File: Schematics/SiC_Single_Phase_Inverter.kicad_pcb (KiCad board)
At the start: 2 copper layers, 200 x 84 mm, 51 parts, among them J1 23AH8785-Black, J2 23AH8786-Red, Q1 STB10NK60ZT4, Q2 STB10NK60ZT4, Q3 C3M0025065K, Q4 C3M0025065K, Q5 C3M0025065K, Q6 C3M0025065K, Q7 C3M0025065K, U1 UCC21710QDWRQ1, U2 UCC21710QDWRQ1, U3 UCC21710QDWRQ1, U4 UCC21710QDWRQ1

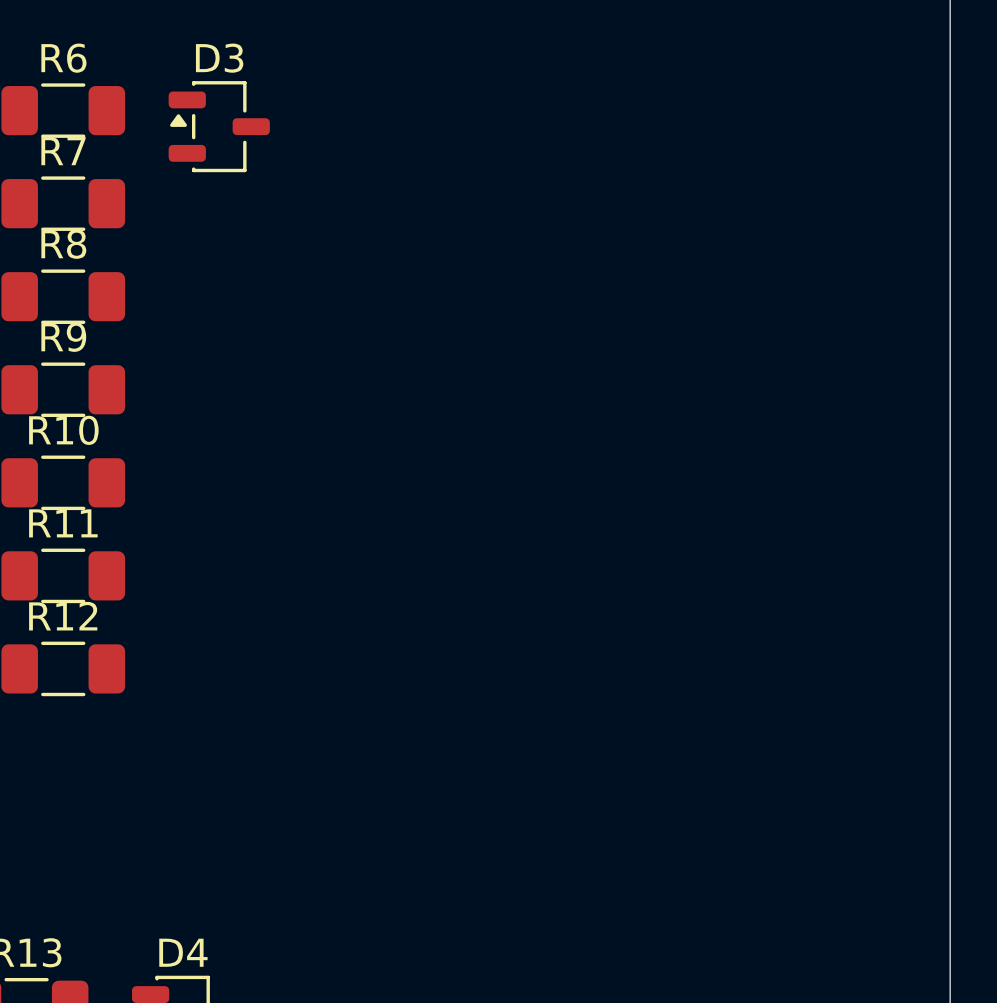
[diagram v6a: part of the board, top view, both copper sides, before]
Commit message: Copy past Leg A onto Leg B, Changed hames on both High/Low side to match Leg B
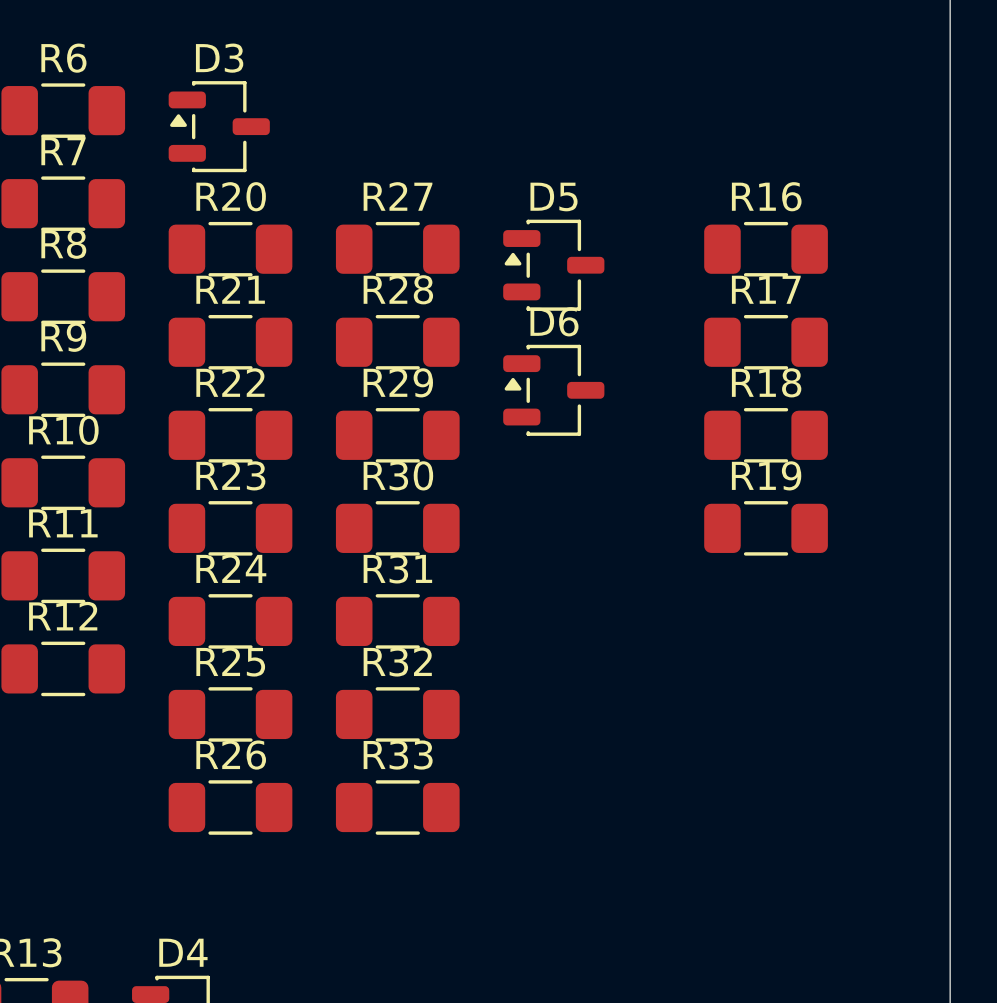
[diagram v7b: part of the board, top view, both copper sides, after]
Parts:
- added D5: BZX84C20-7-F, Package_TO_SOT_SMD:SOT-23-3, F.Cu at (255.9, 57.1)
- added D6: BZX84C20-7-F, Package_TO_SOT_SMD:SOT-23-3, F.Cu at (255.9, 61.6)
- added R16: 5K, Resistor_SMD:R_1206_3216Metric_Pad1.30x1.75mm_HandSolder, F.Cu at (263.4, 56.6)
- added R17: 5K, Resistor_SMD:R_1206_3216Metric_Pad1.30x1.75mm_HandSolder, F.Cu at (263.4, 59.9)
- added R18: 5K, Resistor_SMD:R_1206_3216Metric_Pad1.30x1.75mm_HandSolder, F.Cu at (263.4, 63.2)
- added R19: 5K, Resistor_SMD:R_1206_3216Metric_Pad1.30x1.75mm_HandSolder, F.Cu at (263.4, 66.5)
- added R20: 100K, Resistor_SMD:R_1206_3216Metric_Pad1.30x1.75mm_HandSolder, F.Cu at (244.4, 56.6)
- added R21: 100K, Resistor_SMD:R_1206_3216Metric_Pad1.30x1.75mm_HandSolder, F.Cu at (244.4, 59.9)
- added R22: 10, Resistor_SMD:R_1206_3216Metric_Pad1.30x1.75mm_HandSolder, F.Cu at (244.4, 63.2)
- added R23: 10, Resistor_SMD:R_1206_3216Metric_Pad1.30x1.75mm_HandSolder, F.Cu at (244.4, 66.5)
- added R24: 10, Resistor_SMD:R_1206_3216Metric_Pad1.30x1.75mm_HandSolder, F.Cu at (244.4, 69.8)
- added R25: 10, Resistor_SMD:R_1206_3216Metric_Pad1.30x1.75mm_HandSolder, F.Cu at (244.4, 73.1)
- added R26: 5K, Resistor_SMD:R_1206_3216Metric_Pad1.30x1.75mm_HandSolder, F.Cu at (244.4, 76.4)
- added R27: 100, Resistor_SMD:R_1206_3216Metric_Pad1.30x1.75mm_HandSolder, F.Cu at (250.3, 56.6)
- added R28: 5K, Resistor_SMD:R_1206_3216Metric_Pad1.30x1.75mm_HandSolder, F.Cu at (250.3, 59.9)
- added R29: 5K, Resistor_SMD:R_1206_3216Metric_Pad1.30x1.75mm_HandSolder, F.Cu at (250.3, 63.2)
- added R30: 100, Resistor_SMD:R_1206_3216Metric_Pad1.30x1.75mm_HandSolder, F.Cu at (250.3, 66.5)
- added R31: 5K, Resistor_SMD:R_1206_3216Metric_Pad1.30x1.75mm_HandSolder, F.Cu at (250.3, 69.8)
- added R32: 5K, Resistor_SMD:R_1206_3216Metric_Pad1.30x1.75mm_HandSolder, F.Cu at (250.3, 73.1)
- added R33: 5K, Resistor_SMD:R_1206_3216Metric_Pad1.30x1.75mm_HandSolder, F.Cu at (250.3, 76.4)
- R10, R12: value 10K -> 5K
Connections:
- D4 pad 2: GND -> GND_ISO_LALS
- Q4 pad 1: unconnected-(Q4-Pad1) -> /Full-Bridge/Leg_B_Power_Stage/BUS_DC+
- Q4 pad 2: unconnected-(Q4-Pad2) -> GND_ISO_LAHS
- Q4 pad 3: unconnected-(Q4-Pad3) -> GND_ISO_LAHS
- Q4 pad 4: Net-(Q4-Pad4) -> /Full-Bridge/Leg_B_Power_Stage/LegA_HS_Gate
- Q5 pad 1: unconnected-(Q5-Pad1) -> GND_ISO_LAHS
- Q5 pad 2: unconnected-(Q5-Pad2) -> GND_ISO_LALS
- Q5 pad 3: unconnected-(Q5-Pad3) -> GND_ISO_LALS
- Q5 pad 4: unconnected-(Q5-Pad4) -> /Full-Bridge/Leg_B_Power_Stage/LegA_LS_Gate
- Q7 pad 2: GND -> GND_ISO_LALS
- Q7 pad 3: GND -> GND_ISO_LALS
- R10 pad 1: /Full-Bridge/Leg_A_Power_Stage/LS_LegA_EN -> +3V3
- R10 pad 2: +3V3 -> /Full-Bridge/Leg_A_Power_Stage/LS_LegA_EN
- R12 pad 1: /Full-Bridge/Leg_A_Power_Stage/HS_LegA_EN -> +3V3
- R12 pad 2: +3V3 -> /Full-Bridge/Leg_A_Power_Stage/HS_LegA_EN
- R8 pad 2: GND -> GND_ISO_LALS
- U2 pad 1: GND -> GND_ISO_LALS
- U2 pad 2: GND -> GND_ISO_LALS
- U2 pad 3: GND -> GND_ISO_LALS
- U2 pad 5: +15V_LALS -> +15V_ISO_LALS
- U2 pad 8: /Full-Bridge/Leg_A_Power_Stage/GND_ISO_LALS -> GND_ISO_LALS
- U3 pad 1: unconnected-(U3-AIN-Pad1) -> GND_ISO_LALS
- U3 pad 10: unconnected-(U3-IN+-Pad10) -> Net-(U3-IN+)
- U3 pad 11: unconnected-(U3-IN--Pad11) -> LOGIC_GND
- U3 pad 12: unconnected-(U3-RDY-Pad12) -> /Full-Bridge/Leg_B_Power_Stage/LS_LegB_RDY
- U3 pad 13: unconnected-(U3-~{FLT}-Pad13) -> /Full-Bridge/Leg_B_Power_Stage/~{LS_LegB_FLT}
- U3 pad 14: unconnected-(U3-~{RST}/EN-Pad14) -> /Full-Bridge/Leg_B_Power_Stage/LS_LegB_EN
- U3 pad 15: unconnected-(U3-VCC-Pad15) -> +3V3
- U3 pad 2: unconnected-(U3-OC-Pad2) -> GND_ISO_LALS
- U3 pad 3: unconnected-(U3-COM-Pad3) -> GND_ISO_LALS
- U3 pad 4: unconnected-(U3-OUTH-Pad4) -> /Full-Bridge/Leg_B_Power_Stage/LegA_LS_OUTH
- U3 pad 5: unconnected-(U3-VDD-Pad5) -> +15V_ISO_LALS
- U3 pad 6: unconnected-(U3-OUTL-Pad6) -> /Full-Bridge/Leg_B_Power_Stage/LegA_LS_OUTL
- U3 pad 7: unconnected-(U3-CLMPI-Pad7) -> /Full-Bridge/Leg_B_Power_Stage/LegA_LS_Gate
- U3 pad 8: unconnected-(U3-VEE-Pad8) -> GND_ISO_LALS
- U3 pad 9: unconnected-(U3-GND-Pad9) -> LOGIC_GND
- U4 pad 1: unconnected-(U4-AIN-Pad1) -> GND_ISO_LAHS
- U4 pad 10: unconnected-(U4-IN+-Pad10) -> Net-(U4-IN+)
- U4 pad 11: unconnected-(U4-IN--Pad11) -> LOGIC_GND
- U4 pad 12: unconnected-(U4-RDY-Pad12) -> /Full-Bridge/Leg_B_Power_Stage/HS_LegB_RDY
- U4 pad 13: unconnected-(U4-~{FLT}-Pad13) -> /Full-Bridge/Leg_B_Power_Stage/~{HS_LegB_FLT}
- U4 pad 14: unconnected-(U4-~{RST}/EN-Pad14) -> /Full-Bridge/Leg_B_Power_Stage/HS_LegB_EN
- U4 pad 15: unconnected-(U4-VCC-Pad15) -> +3V3
- U4 pad 2: unconnected-(U4-OC-Pad2) -> GND_ISO_LAHS
- U4 pad 3: unconnected-(U4-COM-Pad3) -> GND_ISO_LAHS
- U4 pad 4: unconnected-(U4-OUTH-Pad4) -> /Full-Bridge/Leg_B_Power_Stage/LegA_HS_OUTH
- U4 pad 5: unconnected-(U4-VDD-Pad5) -> +15V__ISO_LAHS
- U4 pad 6: unconnected-(U4-OUTL-Pad6) -> /Full-Bridge/Leg_B_Power_Stage/LegA_HS_OUTL
- U4 pad 7: unconnected-(U4-CLMPI-Pad7) -> /Full-Bridge/Leg_B_Power_Stage/LegA_HS_Gate
- U4 pad 8: unconnected-(U4-VEE-Pad8) -> GND_ISO_LAHS
- U4 pad 9: unconnected-(U4-GND-Pad9) -> LOGIC_GND

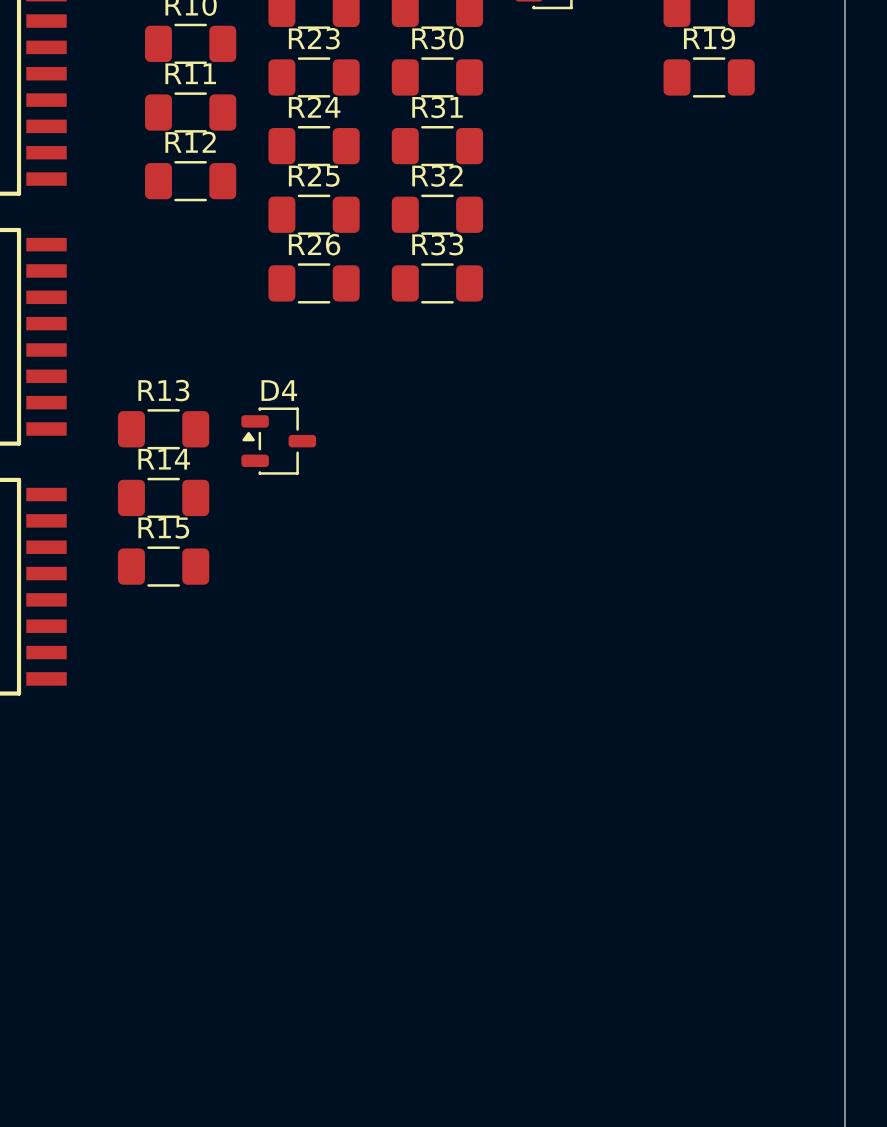
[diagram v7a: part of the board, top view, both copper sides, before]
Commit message: Added Footprints for Cap size 15u, 1u, 0.1u and 100p
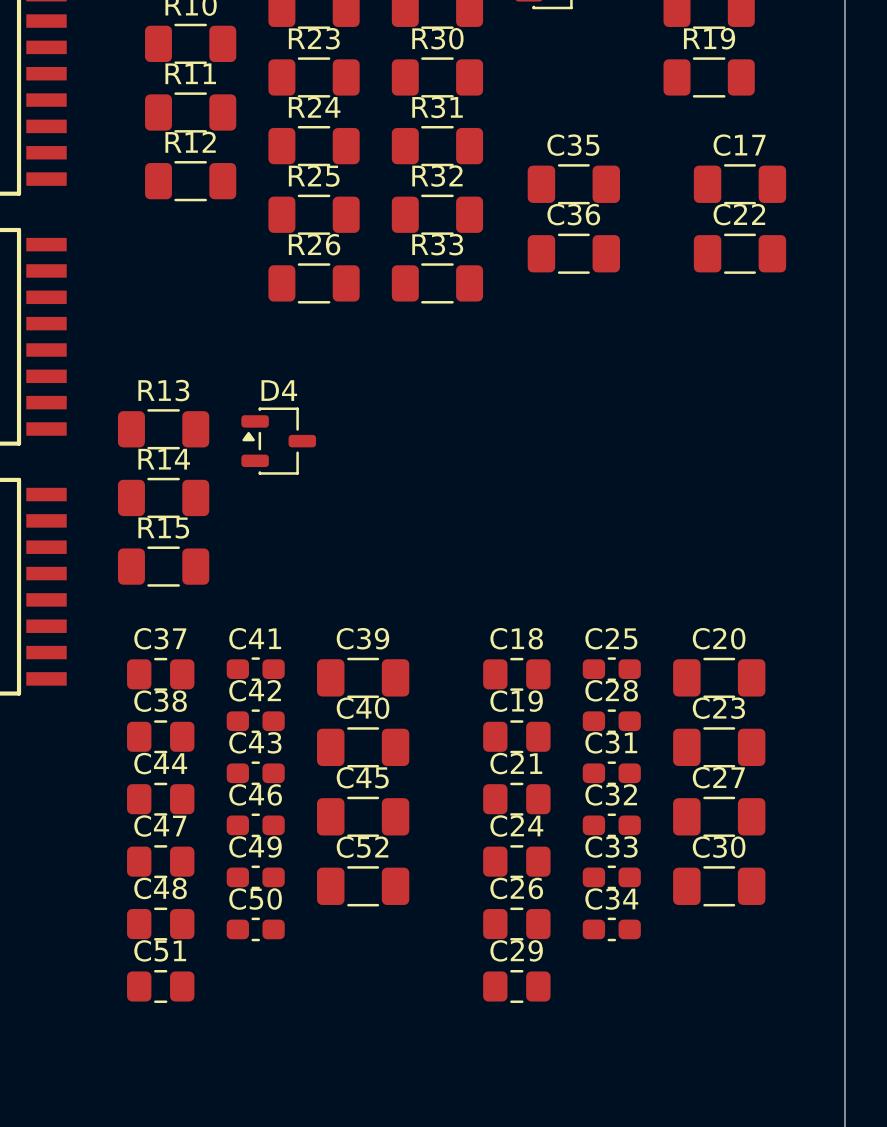
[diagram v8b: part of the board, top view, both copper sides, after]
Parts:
- added C17: 15 u, Capacitor_SMD:C_1206_3216Metric_Pad1.33x1.80mm_HandSolder, F.Cu at (264.9, 71.7)
- added C18: 0.1 u, Capacitor_SMD:C_0805_2012Metric_Pad1.18x1.45mm_HandSolder, F.Cu at (254.2, 95.3)
- added C19: 0.1 u, Capacitor_SMD:C_0805_2012Metric_Pad1.18x1.45mm_HandSolder, F.Cu at (254.2, 98.3)
- added C20: 1 u, Capacitor_SMD:C_1206_3216Metric_Pad1.33x1.80mm_HandSolder, F.Cu at (263.9, 95.5)
- added C21: 0.1 u, Capacitor_SMD:C_0805_2012Metric_Pad1.18x1.45mm_HandSolder, F.Cu at (254.2, 101.3)
- added C22: 15 u, Capacitor_SMD:C_1206_3216Metric_Pad1.33x1.80mm_HandSolder, F.Cu at (264.9, 75.0)
- added C23: 1 u, Capacitor_SMD:C_1206_3216Metric_Pad1.33x1.80mm_HandSolder, F.Cu at (263.9, 98.8)
- added C24: 0.1 u, Capacitor_SMD:C_0805_2012Metric_Pad1.18x1.45mm_HandSolder, F.Cu at (254.2, 104.3)
- added C25: 100 p, Capacitor_SMD:C_0603_1608Metric_Pad1.08x0.95mm_HandSolder, F.Cu at (258.8, 95.0)
- added C26: 0.1 u, Capacitor_SMD:C_0805_2012Metric_Pad1.18x1.45mm_HandSolder, F.Cu at (254.2, 107.3)
- added C27: 1 u, Capacitor_SMD:C_1206_3216Metric_Pad1.33x1.80mm_HandSolder, F.Cu at (263.9, 102.2)
- added C28: 100 p, Capacitor_SMD:C_0603_1608Metric_Pad1.08x0.95mm_HandSolder, F.Cu at (258.8, 97.5)
- added C29: 0.1 u, Capacitor_SMD:C_0805_2012Metric_Pad1.18x1.45mm_HandSolder, F.Cu at (254.2, 110.3)
- added C30: 1 u, Capacitor_SMD:C_1206_3216Metric_Pad1.33x1.80mm_HandSolder, F.Cu at (263.9, 105.5)
- added C31: 100 p, Capacitor_SMD:C_0603_1608Metric_Pad1.08x0.95mm_HandSolder, F.Cu at (258.8, 100.0)
- added C32: 100 p, Capacitor_SMD:C_0603_1608Metric_Pad1.08x0.95mm_HandSolder, F.Cu at (258.8, 102.6)
- added C33: 100 p, Capacitor_SMD:C_0603_1608Metric_Pad1.08x0.95mm_HandSolder, F.Cu at (258.8, 105.1)
- added C34: 100 p, Capacitor_SMD:C_0603_1608Metric_Pad1.08x0.95mm_HandSolder, F.Cu at (258.8, 107.6)
- added C35: 15 u, Capacitor_SMD:C_1206_3216Metric_Pad1.33x1.80mm_HandSolder, F.Cu at (256.9, 71.7)
- added C36: 15 u, Capacitor_SMD:C_1206_3216Metric_Pad1.33x1.80mm_HandSolder, F.Cu at (256.9, 75.0)
- added C37: 0.1 u, Capacitor_SMD:C_0805_2012Metric_Pad1.18x1.45mm_HandSolder, F.Cu at (237.0, 95.3)
- added C38: 0.1 u, Capacitor_SMD:C_0805_2012Metric_Pad1.18x1.45mm_HandSolder, F.Cu at (237.0, 98.3)
- added C39: 1 u, Capacitor_SMD:C_1206_3216Metric_Pad1.33x1.80mm_HandSolder, F.Cu at (246.8, 95.5)
- added C40: 1 u, Capacitor_SMD:C_1206_3216Metric_Pad1.33x1.80mm_HandSolder, F.Cu at (246.8, 98.8)
- added C41: 100 p, Capacitor_SMD:C_0603_1608Metric_Pad1.08x0.95mm_HandSolder, F.Cu at (241.6, 95.0)
- added C42: 100 p, Capacitor_SMD:C_0603_1608Metric_Pad1.08x0.95mm_HandSolder, F.Cu at (241.6, 97.5)
- added C43: 100 p, Capacitor_SMD:C_0603_1608Metric_Pad1.08x0.95mm_HandSolder, F.Cu at (241.6, 100.0)
- added C44: 0.1 u, Capacitor_SMD:C_0805_2012Metric_Pad1.18x1.45mm_HandSolder, F.Cu at (237.0, 101.3)
- added C45: 1 u, Capacitor_SMD:C_1206_3216Metric_Pad1.33x1.80mm_HandSolder, F.Cu at (246.8, 102.2)
- added C46: 100 p, Capacitor_SMD:C_0603_1608Metric_Pad1.08x0.95mm_HandSolder, F.Cu at (241.6, 102.6)
- added C47: 0.1 u, Capacitor_SMD:C_0805_2012Metric_Pad1.18x1.45mm_HandSolder, F.Cu at (237.0, 104.3)
- added C48: 0.1 u, Capacitor_SMD:C_0805_2012Metric_Pad1.18x1.45mm_HandSolder, F.Cu at (237.0, 107.3)
- added C49: 100 p, Capacitor_SMD:C_0603_1608Metric_Pad1.08x0.95mm_HandSolder, F.Cu at (241.6, 105.1)
- added C50: 100 p, Capacitor_SMD:C_0603_1608Metric_Pad1.08x0.95mm_HandSolder, F.Cu at (241.6, 107.6)
- added C51: 0.1 u, Capacitor_SMD:C_0805_2012Metric_Pad1.18x1.45mm_HandSolder, F.Cu at (237.0, 110.3)
- added C52: 1 u, Capacitor_SMD:C_1206_3216Metric_Pad1.33x1.80mm_HandSolder, F.Cu at (246.8, 105.5)
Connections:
- net /Full-Bridge/Leg_A_Power_Stage/HS_LegA_EN renamed /Full-Bridge/HS_LegA_EN
- net /Full-Bridge/Leg_A_Power_Stage/HS_LegA_RDY renamed /Full-Bridge/HS_LegA_RDY
- net /Full-Bridge/Leg_A_Power_Stage/LS_LegA_EN renamed /Full-Bridge/LS_LegA_EN
- net /Full-Bridge/Leg_A_Power_Stage/LS_LegA_RDY renamed /Full-Bridge/LS_LegA_RDY
- net /Full-Bridge/Leg_A_Power_Stage/PWM_A_H renamed /Full-Bridge/PWM_A_H
- net /Full-Bridge/Leg_A_Power_Stage/PWM_A_L renamed /Full-Bridge/PWM_A_L
- net /Full-Bridge/Leg_A_Power_Stage/~{HS_LegA_FLT} renamed /Full-Bridge/~{HS_LegA_FLT}
- net /Full-Bridge/Leg_A_Power_Stage/~{LS_LegA_FLT} renamed /Full-Bridge/~{LS_LegA_FLT}
- net /Full-Bridge/Leg_B_Power_Stage/HS_LegB_EN renamed /Full-Bridge/HS_LegB_EN
- net /Full-Bridge/Leg_B_Power_Stage/HS_LegB_RDY renamed /Full-Bridge/HS_LegB_RDY
- net /Full-Bridge/Leg_B_Power_Stage/LS_LegB_EN renamed /Full-Bridge/LS_LegB_EN
- net /Full-Bridge/Leg_B_Power_Stage/LS_LegB_RDY renamed /Full-Bridge/LS_LegB_RDY
- net /Full-Bridge/Leg_B_Power_Stage/LegA_HS_Gate renamed /Full-Bridge/Leg_B_Power_Stage/LegB_HS_Gate
- net /Full-Bridge/Leg_B_Power_Stage/LegA_HS_OUTH renamed /Full-Bridge/Leg_B_Power_Stage/LegB_HS_OUTH
- net /Full-Bridge/Leg_B_Power_Stage/LegA_HS_OUTL renamed /Full-Bridge/Leg_B_Power_Stage/LegB_HS_OUTL
- net /Full-Bridge/Leg_B_Power_Stage/LegA_LS_Gate renamed /Full-Bridge/Leg_B_Power_Stage/LegB_LS_Gate
- net /Full-Bridge/Leg_B_Power_Stage/LegA_LS_OUTH renamed /Full-Bridge/Leg_B_Power_Stage/LegB_LS_OUTH
- net /Full-Bridge/Leg_B_Power_Stage/LegA_LS_OUTL renamed /Full-Bridge/Leg_B_Power_Stage/LegB_LS_OUTL
- net /Full-Bridge/Leg_B_Power_Stage/PWM_B_H renamed /Full-Bridge/PWM_B_H
- net /Full-Bridge/Leg_B_Power_Stage/PWM_B_L renamed /Full-Bridge/PWM_B_L
- net /Full-Bridge/Leg_B_Power_Stage/~{HS_LegB_FLT} renamed /Full-Bridge/~{HS_LegB_FLT}
- net /Full-Bridge/Leg_B_Power_Stage/~{LS_LegB_FLT} renamed /Full-Bridge/~{LS_LegB_FLT}
- D5 pad 2: GND_ISO_LAHS -> GND_ISO_LBHS
- D6 pad 2: GND_ISO_LALS -> GND_ISO_LBLS
- Q3 pad 1: /Full-Bridge/Leg_A_Power_Stage/BUS_DC+ -> /Full-Bridge/BUS_DC+
- Q4 pad 1: /Full-Bridge/Leg_B_Power_Stage/BUS_DC+ -> /Full-Bridge/BUS_DC+
- Q4 pad 2: GND_ISO_LAHS -> GND_ISO_LBHS
- Q4 pad 3: GND_ISO_LAHS -> GND_ISO_LBHS
- Q5 pad 1: GND_ISO_LAHS -> GND_ISO_LBHS
- Q5 pad 2: GND_ISO_LALS -> GND_ISO_LBLS
- Q5 pad 3: GND_ISO_LALS -> GND_ISO_LBLS
- R20 pad 2: GND_ISO_LAHS -> GND_ISO_LBHS
- R21 pad 2: GND_ISO_LALS -> GND_ISO_LBLS
- U3 pad 1: GND_ISO_LALS -> GND_ISO_LBLS
- U3 pad 2: GND_ISO_LALS -> GND_ISO_LBLS
- U3 pad 3: GND_ISO_LALS -> GND_ISO_LBLS
- U3 pad 5: +15V_ISO_LALS -> +15V_ISO_LBLS
- U3 pad 8: GND_ISO_LALS -> GND_ISO_LBLS
- U4 pad 1: GND_ISO_LAHS -> GND_ISO_LBHS
- U4 pad 2: GND_ISO_LAHS -> GND_ISO_LBHS
- U4 pad 3: GND_ISO_LAHS -> GND_ISO_LBHS
- U4 pad 5: +15V__ISO_LAHS -> +15V__ISO_LBHS
- U4 pad 8: GND_ISO_LAHS -> GND_ISO_LBHS
